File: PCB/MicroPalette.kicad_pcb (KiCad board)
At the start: 2 copper layers, 85 x 30 mm, 12 parts, among them J1 Conn_01x07_Pin, J2 Conn_01x04_Pin, U1 XIAO-RP2040-DIP

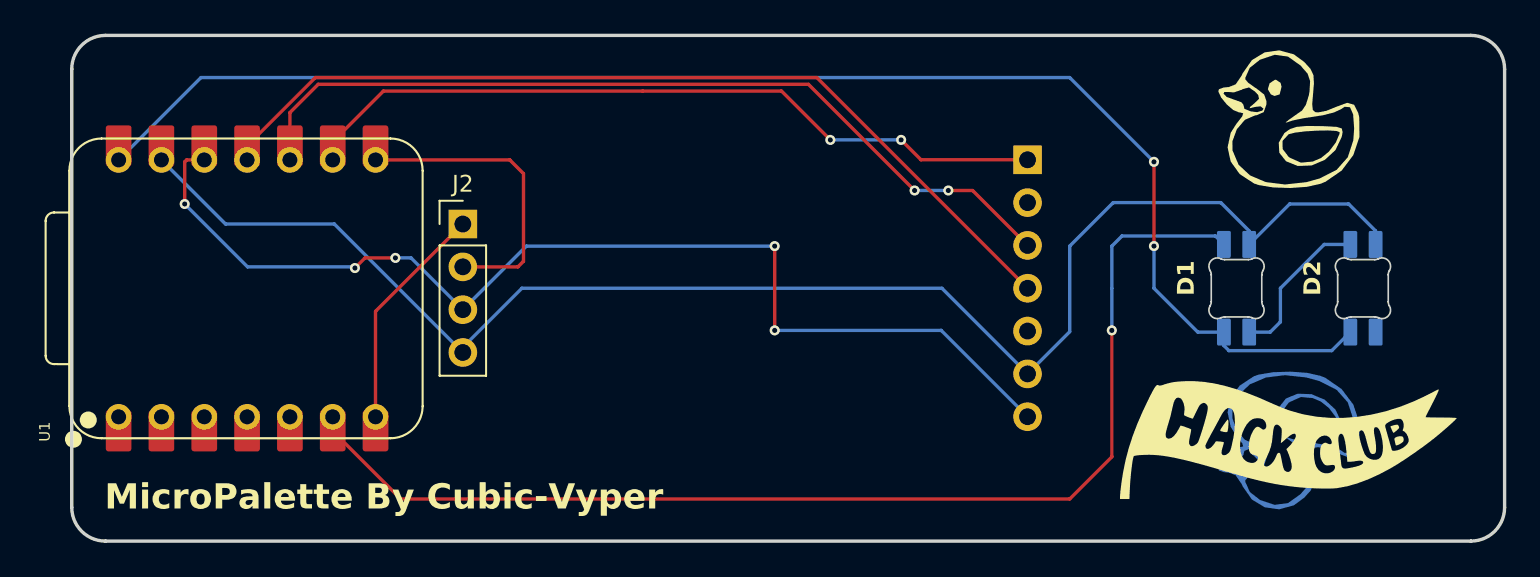
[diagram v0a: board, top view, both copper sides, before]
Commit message: Add files via upload
fixed pcb, sda/scl was wrong in the previous version
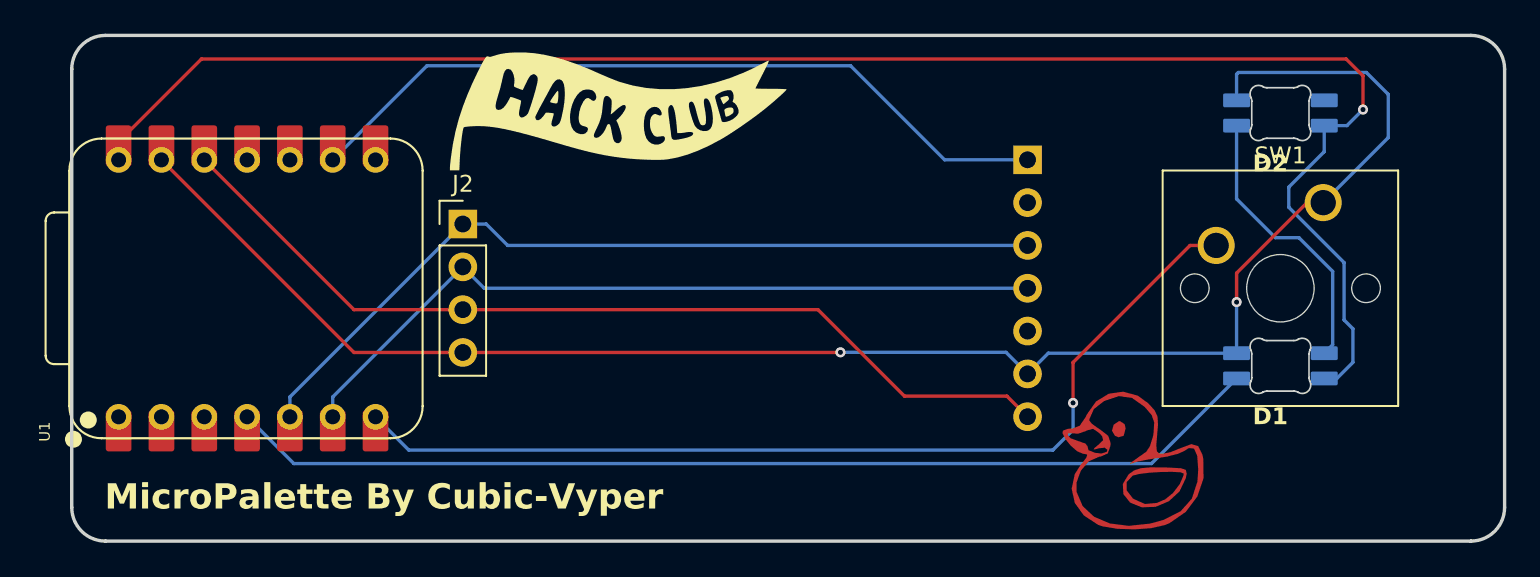
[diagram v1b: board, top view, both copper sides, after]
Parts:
- added SW1: SW_Push, Button_Switch_Keyboard:SW_Cherry_MX_1.00u_PCB, F.Cu at (150.0, 54.9)
- G*** (x4): moved to B.Cu
- moved G*** 44.9 mm to (107.8, 70.0)
- moved G*** 44.3 mm to (108.2, 49.5)
- moved G*** 21.3 mm to (155.2, 70.0)
- moved G*** 13.5 mm to (106.0, 52.5)
- moved D2 11.6 mm to (147.5, 49.5), turned to 180 degrees
- moved G*** 9.33 mm to (138.8, 70.2) (x3)
- moved D1 5.15 mm to (147.5, 64.5), turned to 180 degrees
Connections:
- J1 pad 3: D2 -> SDA
- J1 pad 4: D1 -> SCL
- J2 pad 1: D5 -> SDA
- J2 pad 2: D4 -> SCL
- U1 pad 10: D2 -> unconnected-(U1-GPIO4/MISO-Pad10)
- U1 pad 11: D1 -> unconnected-(U1-GPIO3/MOSI-Pad11)
- U1 pad 4: unconnected-(U1-GPIO29/ADC3/A3-Pad4) -> D6
- U1 pad 5: unconnected-(U1-GPIO6/SDA-Pad5) -> SDA
- U1 pad 6: D6 -> SCL
- U1 pad 7: D5 -> D7
- U1 pad 8: D4 -> unconnected-(U1-GPIO1/RX-Pad8)
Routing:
- net D7: track 0.00 -> 58.1 mm, vias 0 -> 1
- net D1: track 54.0 -> 0.00 mm
- net D2: track 51.2 -> 0.00 mm, vias 2 -> 0
- net SDA: track 0.00 -> 49.7 mm
- net SCL: track 0.00 -> 46.1 mm
- net D4: track 18.1 -> 0.00 mm
- net D5: track 13.6 -> 0.00 mm
- net +5V: track 87.1 -> 100.6 mm, vias 2 -> 1
- net +3V3: track 65.5 -> 55.1 mm, vias 5 -> 0
- net GND: track 91.8 -> 100.3 mm, vias 0 -> 2
- net Net-(D1-DOUT): track 9.33 -> 16.9 mm
- net D6: track 69.4 -> 61.9 mm, vias 1 -> 0
- net D3: track 45.2 -> 45.8 mm, vias 2 -> 0
